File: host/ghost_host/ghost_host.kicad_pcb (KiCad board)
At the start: 2 copper layers, 13 parts, among them J14 Conn_01x04, J15 RJ12_Shielded, J16 Conn_01x06, U6 PCA9615DP

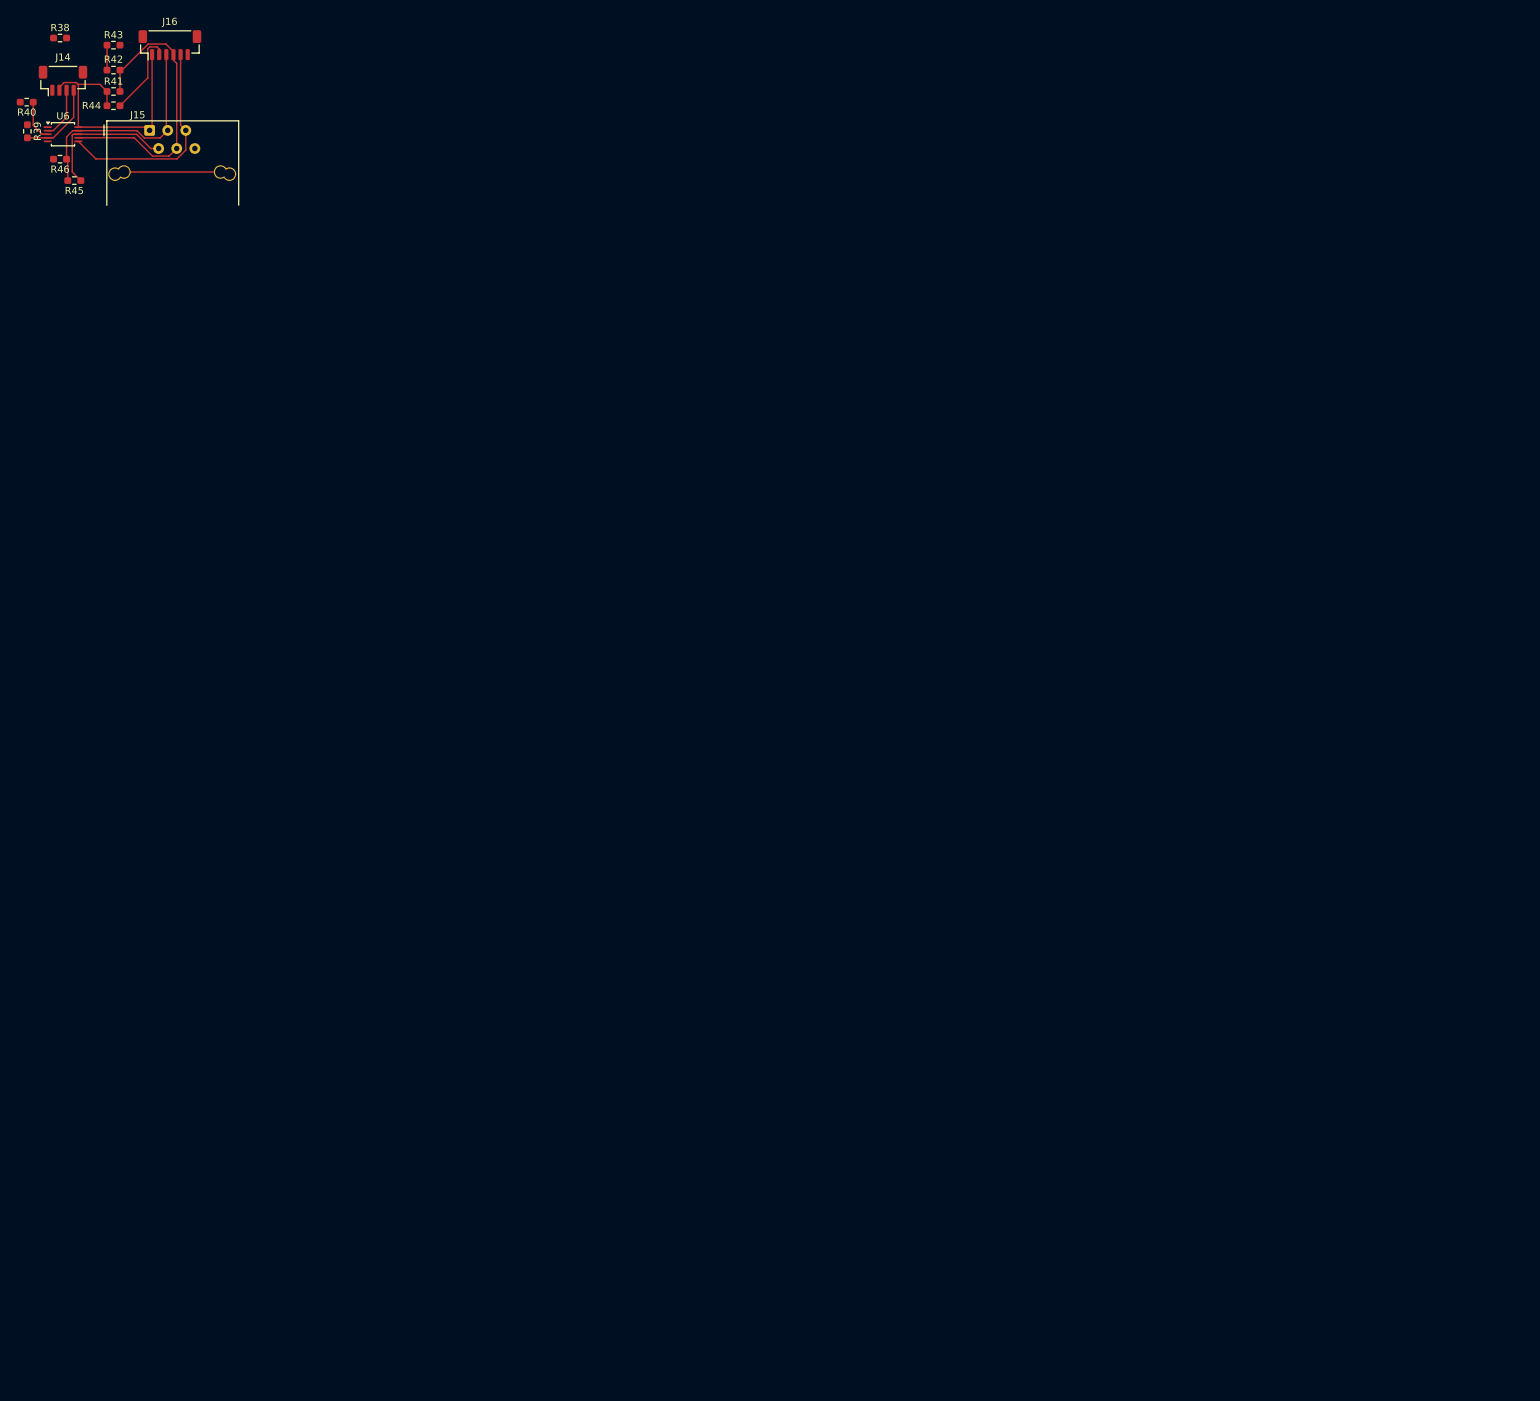
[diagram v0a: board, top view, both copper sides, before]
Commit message: finished host board PCB layout
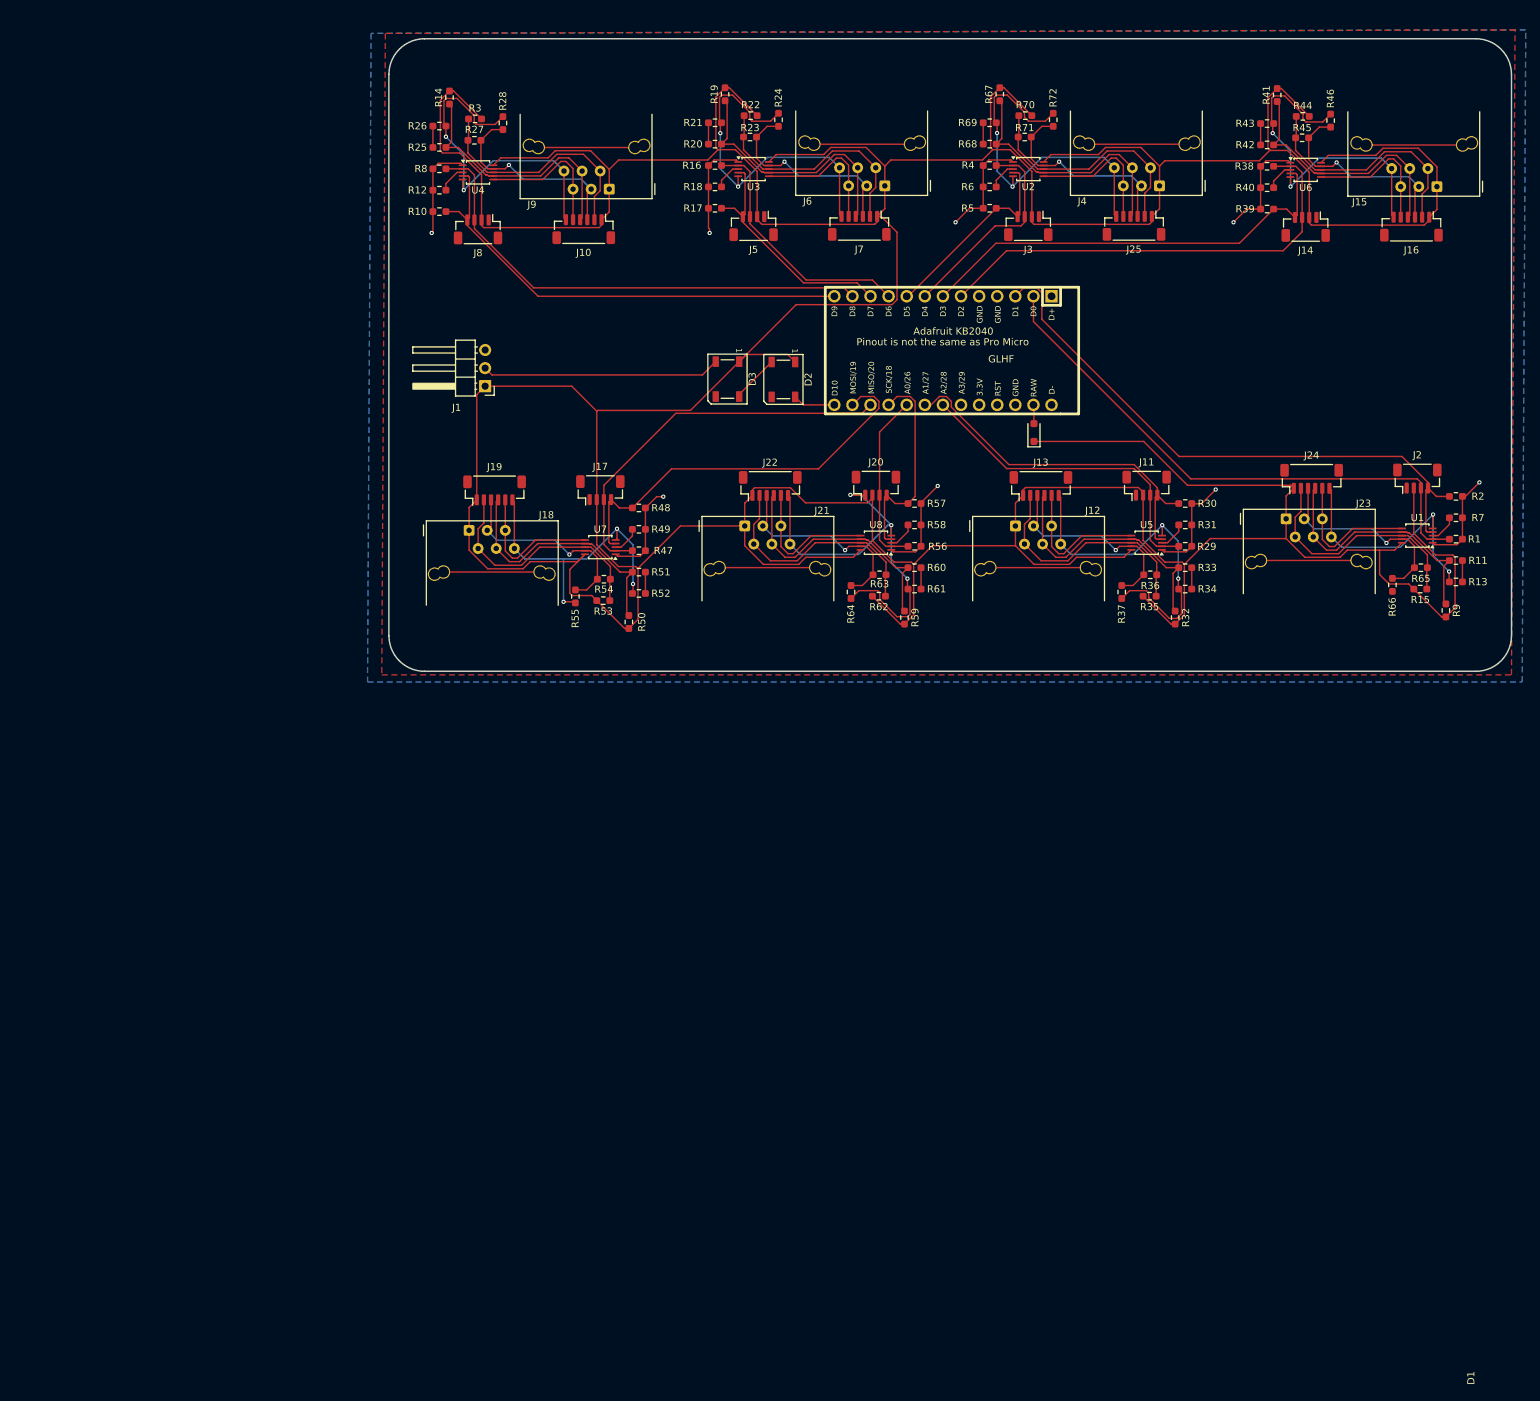
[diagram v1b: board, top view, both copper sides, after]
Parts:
- added D1: CMS06(TE12L,Q,M), Diode_SMD:D_SOD-323_HandSoldering, F.Cu at (165.0, 89.5)
- added D2: WS2812B, LED_SMD:LED_WS2812B_PLCC4_5.0x5.0mm_P3.2mm, F.Cu at (129.8, 82.0)
- added D3: WS2812B, LED_SMD:LED_WS2812B_PLCC4_5.0x5.0mm_P3.2mm, F.Cu at (122.0, 82.0)
- added J1: RGB_3_Pin_Connector, Connector_PinHeader_2.54mm:PinHeader_1x03_P2.54mm_Horizontal, F.Cu at (88.0, 83.0)
- added J10: Conn_01x06, Connector_JST:JST_SH_BM06B-SRSS-TB_1x06-1MP_P1.00mm_Vertical, F.Cu at (101.8, 61.0)
- added J11: Conn_01x04, Connector_JST:JST_SH_BM04B-SRSS-TB_1x04-1MP_P1.00mm_Vertical, F.Cu at (180.8, 97.0)
- added J12: RJ12_Shielded, RJ12_Pin_Connector:RJ12_Pin_Connector, F.Cu at (162.4, 102.6)
- added J13: Conn_01x06, Connector_JST:JST_SH_BM06B-SRSS-TB_1x06-1MP_P1.00mm_Vertical, F.Cu at (166.0, 97.0)
- added J17: Conn_01x04, Connector_JST:JST_SH_BM04B-SRSS-TB_1x04-1MP_P1.00mm_Vertical, F.Cu at (104.2, 97.6)
- added J18: RJ12_Shielded, RJ12_Pin_Connector:RJ12_Pin_Connector, F.Cu at (85.8, 103.2)
- added J19: Conn_01x06, Connector_JST:JST_SH_BM06B-SRSS-TB_1x06-1MP_P1.00mm_Vertical, F.Cu at (89.3, 97.6)
- added J2: Conn_01x04, Connector_JST:JST_SH_BM04B-SRSS-TB_1x04-1MP_P1.00mm_Vertical, F.Cu at (218.8, 96.0)
- added J20: Conn_01x04, Connector_JST:JST_SH_BM04B-SRSS-TB_1x04-1MP_P1.00mm_Vertical, F.Cu at (142.8, 97.0)
- added J21: RJ12_Shielded, RJ12_Pin_Connector:RJ12_Pin_Connector, F.Cu at (124.4, 102.6)
- added J22: Conn_01x06, Connector_JST:JST_SH_BM06B-SRSS-TB_1x06-1MP_P1.00mm_Vertical, F.Cu at (128.0, 97.0)
- added J23: RJ12_Shielded, RJ12_Pin_Connector:RJ12_Pin_Connector, F.Cu at (200.4, 101.6)
- added J24: Conn_01x06, Connector_JST:JST_SH_BM06B-SRSS-TB_1x06-1MP_P1.00mm_Vertical, F.Cu at (204.0, 96.0)
- added J25: Conn_01x06, Connector_JST:JST_SH_BM06B-SRSS-TB_1x06-1MP_P1.00mm_Vertical, F.Cu at (179.0, 60.5)
- added J3: Conn_01x04, Connector_JST:JST_SH_BM04B-SRSS-TB_1x04-1MP_P1.00mm_Vertical, F.Cu at (164.2, 60.5)
- added J4: RJ12_Shielded, RJ12_Pin_Connector:RJ12_Pin_Connector, F.Cu at (182.6, 54.9)
- added J5: Conn_01x04, Connector_JST:JST_SH_BM04B-SRSS-TB_1x04-1MP_P1.00mm_Vertical, F.Cu at (125.7, 60.5)
- added J6: RJ12_Shielded, RJ12_Pin_Connector:RJ12_Pin_Connector, F.Cu at (144.1, 54.9)
- added J7: Conn_01x06, Connector_JST:JST_SH_BM06B-SRSS-TB_1x06-1MP_P1.00mm_Vertical, F.Cu at (140.5, 60.5)
- added J8: Conn_01x04, Connector_JST:JST_SH_BM04B-SRSS-TB_1x04-1MP_P1.00mm_Vertical, F.Cu at (87.0, 61.0)
- added J9: RJ12_Shielded, RJ12_Pin_Connector:RJ12_Pin_Connector, F.Cu at (105.4, 55.4)
- added R1: 4.7k, Resistor_SMD:R_0603_1608Metric_Pad0.98x0.95mm_HandSolder, F.Cu at (224.2, 104.5)
- added R10: 4.7k, Resistor_SMD:R_0603_1608Metric_Pad0.98x0.95mm_HandSolder, F.Cu at (81.6, 58.5)
- added R11: 120, Resistor_SMD:R_0603_1608Metric_Pad0.98x0.95mm_HandSolder, F.Cu at (224.2, 107.5)
- added R12: 10k, Resistor_SMD:R_0603_1608Metric_Pad0.98x0.95mm_HandSolder, F.Cu at (81.6, 55.5)
- added R13: 600, Resistor_SMD:R_0603_1608Metric_Pad0.98x0.95mm_HandSolder, F.Cu at (224.2, 110.5)
- added R14: 600, Resistor_SMD:R_0603_1608Metric_Pad0.98x0.95mm_HandSolder, F.Cu at (83.0, 42.5)
- added R15: 600, Resistor_SMD:R_0603_1608Metric_Pad0.98x0.95mm_HandSolder, F.Cu at (219.2, 111.5)
- added R16: 4.7k, Resistor_SMD:R_0603_1608Metric_Pad0.98x0.95mm_HandSolder, F.Cu at (120.3, 52.0)
- added R17: 4.7k, Resistor_SMD:R_0603_1608Metric_Pad0.98x0.95mm_HandSolder, F.Cu at (120.3, 58.0)
- added R18: 10k, Resistor_SMD:R_0603_1608Metric_Pad0.98x0.95mm_HandSolder, F.Cu at (120.3, 55.0)
- added R19: 600, Resistor_SMD:R_0603_1608Metric_Pad0.98x0.95mm_HandSolder, F.Cu at (121.7, 42.0)
- added R2: 4.7k, Resistor_SMD:R_0603_1608Metric_Pad0.98x0.95mm_HandSolder, F.Cu at (224.2, 98.5)
- added R20: 120, Resistor_SMD:R_0603_1608Metric_Pad0.98x0.95mm_HandSolder, F.Cu at (120.3, 49.0)
- added R21: 600, Resistor_SMD:R_0603_1608Metric_Pad0.98x0.95mm_HandSolder, F.Cu at (120.3, 46.0)
- added R22: 600, Resistor_SMD:R_0603_1608Metric_Pad0.98x0.95mm_HandSolder, F.Cu at (125.3, 45.0)
- added R23: 120, Resistor_SMD:R_0603_1608Metric_Pad0.98x0.95mm_HandSolder, F.Cu at (125.2, 48.0)
- added R24: 600, Resistor_SMD:R_0603_1608Metric_Pad0.98x0.95mm_HandSolder, F.Cu at (129.2, 45.6)
- added R25: 120, Resistor_SMD:R_0603_1608Metric_Pad0.98x0.95mm_HandSolder, F.Cu at (81.6, 49.5)
- added R26: 600, Resistor_SMD:R_0603_1608Metric_Pad0.98x0.95mm_HandSolder, F.Cu at (81.6, 46.5)
- added R27: 120, Resistor_SMD:R_0603_1608Metric_Pad0.98x0.95mm_HandSolder, F.Cu at (86.5, 48.5)
- added R28: 600, Resistor_SMD:R_0603_1608Metric_Pad0.98x0.95mm_HandSolder, F.Cu at (90.5, 46.1)
- added R29: 4.7k, Resistor_SMD:R_0603_1608Metric_Pad0.98x0.95mm_HandSolder, F.Cu at (186.2, 105.5)
- added R3: 600, Resistor_SMD:R_0603_1608Metric_Pad0.98x0.95mm_HandSolder, F.Cu at (86.6, 45.5)
- added R30: 4.7k, Resistor_SMD:R_0603_1608Metric_Pad0.98x0.95mm_HandSolder, F.Cu at (186.2, 99.5)
- added R31: 10k, Resistor_SMD:R_0603_1608Metric_Pad0.98x0.95mm_HandSolder, F.Cu at (186.2, 102.5)
- added R32: 600, Resistor_SMD:R_0603_1608Metric_Pad0.98x0.95mm_HandSolder, F.Cu at (184.8, 115.5)
- added R33: 120, Resistor_SMD:R_0603_1608Metric_Pad0.98x0.95mm_HandSolder, F.Cu at (186.2, 108.5)
- added R34: 600, Resistor_SMD:R_0603_1608Metric_Pad0.98x0.95mm_HandSolder, F.Cu at (186.2, 111.5)
- added R35: 600, Resistor_SMD:R_0603_1608Metric_Pad0.98x0.95mm_HandSolder, F.Cu at (181.2, 112.5)
- added R36: 120, Resistor_SMD:R_0603_1608Metric_Pad0.98x0.95mm_HandSolder, F.Cu at (181.3, 109.5)
- added R37: 600, Resistor_SMD:R_0603_1608Metric_Pad0.98x0.95mm_HandSolder, F.Cu at (177.3, 111.9)
- added R4: 4.7k, Resistor_SMD:R_0603_1608Metric_Pad0.98x0.95mm_HandSolder, F.Cu at (158.8, 52.0)
- added R47: 4.7k, Resistor_SMD:R_0603_1608Metric_Pad0.98x0.95mm_HandSolder, F.Cu at (109.6, 106.1)
- added R48: 4.7k, Resistor_SMD:R_0603_1608Metric_Pad0.98x0.95mm_HandSolder, F.Cu at (109.6, 100.1)
- added R49: 10k, Resistor_SMD:R_0603_1608Metric_Pad0.98x0.95mm_HandSolder, F.Cu at (109.6, 103.1)
- added R5: 4.7k, Resistor_SMD:R_0603_1608Metric_Pad0.98x0.95mm_HandSolder, F.Cu at (158.8, 58.0)
- added R50: 600, Resistor_SMD:R_0603_1608Metric_Pad0.98x0.95mm_HandSolder, F.Cu at (108.2, 116.1)
- added R51: 120, Resistor_SMD:R_0603_1608Metric_Pad0.98x0.95mm_HandSolder, F.Cu at (109.6, 109.1)
- added R52: 600, Resistor_SMD:R_0603_1608Metric_Pad0.98x0.95mm_HandSolder, F.Cu at (109.6, 112.1)
- added R53: 600, Resistor_SMD:R_0603_1608Metric_Pad0.98x0.95mm_HandSolder, F.Cu at (104.6, 113.1)
- added R54: 120, Resistor_SMD:R_0603_1608Metric_Pad0.98x0.95mm_HandSolder, F.Cu at (104.7, 110.1)
- added R55: 600, Resistor_SMD:R_0603_1608Metric_Pad0.98x0.95mm_HandSolder, F.Cu at (100.7, 112.5)
- added R56: 4.7k, Resistor_SMD:R_0603_1608Metric_Pad0.98x0.95mm_HandSolder, F.Cu at (148.2, 105.5)
- added R57: 4.7k, Resistor_SMD:R_0603_1608Metric_Pad0.98x0.95mm_HandSolder, F.Cu at (148.2, 99.5)
- added R58: 10k, Resistor_SMD:R_0603_1608Metric_Pad0.98x0.95mm_HandSolder, F.Cu at (148.2, 102.5)
- added R59: 600, Resistor_SMD:R_0603_1608Metric_Pad0.98x0.95mm_HandSolder, F.Cu at (146.8, 115.5)
- added R6: 10k, Resistor_SMD:R_0603_1608Metric_Pad0.98x0.95mm_HandSolder, F.Cu at (158.8, 55.0)
- added R60: 120, Resistor_SMD:R_0603_1608Metric_Pad0.98x0.95mm_HandSolder, F.Cu at (148.2, 108.5)
- added R61: 600, Resistor_SMD:R_0603_1608Metric_Pad0.98x0.95mm_HandSolder, F.Cu at (148.2, 111.5)
- added R62: 600, Resistor_SMD:R_0603_1608Metric_Pad0.98x0.95mm_HandSolder, F.Cu at (143.2, 112.5)
- added R63: 120, Resistor_SMD:R_0603_1608Metric_Pad0.98x0.95mm_HandSolder, F.Cu at (143.3, 109.5)
- added R64: 600, Resistor_SMD:R_0603_1608Metric_Pad0.98x0.95mm_HandSolder, F.Cu at (139.3, 111.9)
- added R65: 120, Resistor_SMD:R_0603_1608Metric_Pad0.98x0.95mm_HandSolder, F.Cu at (219.3, 108.5)
- added R66: 600, Resistor_SMD:R_0603_1608Metric_Pad0.98x0.95mm_HandSolder, F.Cu at (215.3, 110.9)
- added R67: 600, Resistor_SMD:R_0603_1608Metric_Pad0.98x0.95mm_HandSolder, F.Cu at (160.2, 42.0)
- added R68: 120, Resistor_SMD:R_0603_1608Metric_Pad0.98x0.95mm_HandSolder, F.Cu at (158.8, 49.0)
- added R69: 600, Resistor_SMD:R_0603_1608Metric_Pad0.98x0.95mm_HandSolder, F.Cu at (158.8, 46.0)
- added R7: 10k, Resistor_SMD:R_0603_1608Metric_Pad0.98x0.95mm_HandSolder, F.Cu at (224.2, 101.5)
- added R70: 600, Resistor_SMD:R_0603_1608Metric_Pad0.98x0.95mm_HandSolder, F.Cu at (163.8, 45.0)
- added R71: 120, Resistor_SMD:R_0603_1608Metric_Pad0.98x0.95mm_HandSolder, F.Cu at (163.7, 48.0)
- added R72: 600, Resistor_SMD:R_0603_1608Metric_Pad0.98x0.95mm_HandSolder, F.Cu at (167.7, 45.6)
- added R8: 4.7k, Resistor_SMD:R_0603_1608Metric_Pad0.98x0.95mm_HandSolder, F.Cu at (81.6, 52.5)
- added R9: 600, Resistor_SMD:R_0603_1608Metric_Pad0.98x0.95mm_HandSolder, F.Cu at (222.8, 114.5)
- added U1: PCA9615DP, Package_SO:TSSOP-10_3x3mm_P0.5mm, F.Cu at (218.8, 104.0)
- added U2: PCA9615DP, Package_SO:TSSOP-10_3x3mm_P0.5mm, F.Cu at (164.2, 52.5)
- added U3: PCA9615DP, Package_SO:TSSOP-10_3x3mm_P0.5mm, F.Cu at (125.7, 52.5)
- added U4: PCA9615DP, Package_SO:TSSOP-10_3x3mm_P0.5mm, F.Cu at (87.0, 53.0)
- added U5: PCA9615DP, Package_SO:TSSOP-10_3x3mm_P0.5mm, F.Cu at (180.8, 105.0)
- added U7: PCA9615DP, Package_SO:TSSOP-10_3x3mm_P0.5mm, F.Cu at (104.2, 105.6)
- added U8: PCA9615DP, Package_SO:TSSOP-10_3x3mm_P0.5mm, F.Cu at (142.8, 105.0)
- added U9: kb2040, kb2040:kb2040, F.Cu at (153.5, 78.0)
- moved J15 180.8 mm to (221.5, 55.0), turned to 180 degrees
- moved R46 178.3 mm to (206.6, 45.7), turned to 90 degrees
- moved J16 176.0 mm to (218.0, 60.6), turned to 180 degrees
- moved J14 175.6 mm to (203.1, 60.6), turned to 180 degrees
- moved R40 174.4 mm to (197.7, 55.1)
- moved U6 174.4 mm to (203.1, 52.6)
- moved R39 174.3 mm to (197.7, 58.1), turned to 0 degrees
- moved R45 172.4 mm to (202.6, 48.1), turned to 0 degrees
- moved R38 170.3 mm to (197.7, 52.1)
- moved R44 166.9 mm to (202.7, 45.1), turned to 180 degrees
- moved R41 163.3 mm to (199.1, 42.1), turned to -90 degrees
- moved R43 162.2 mm to (197.7, 46.1)
- moved R42 162.2 mm to (197.7, 49.1)
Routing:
- net +5V: track 37.2 -> 818.8 mm
- net GND: track 0.00 -> 385.6 mm, vias 0 -> 18
- net +3.3V: track 0.00 -> 114.7 mm, vias 0 -> 8
- net /scl1: track 0.00 -> 83.3 mm
- net /sda1: track 0.00 -> 78.7 mm
- net /sda5: track 0.00 -> 68.8 mm
- net /scl5: track 0.00 -> 67.0 mm
- net /sda2: track 7.23 -> 64.3 mm
- net /scl8: track 0.00 -> 56.5 mm
- net /sda8: track 0.00 -> 54.8 mm
- net /scl2: track 11.5 -> 62.1 mm
- net /scl6: track 0.00 -> 50.6 mm
- net /sda6: track 0.00 -> 45.9 mm
- net Net-(J25-Pin_4): track 0.00 -> 36.1 mm
- net Net-(J13-Pin_4): track 0.00 -> 36.1 mm
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- added copper zone on B.Cu, net +3.3V
- added copper zone on F.Cu, net GND
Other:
- board outline added: 157.5 x 88.8 mm

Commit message: reorg pcb layout
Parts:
- added H1: MountingHole_Pad, MountingHole:MountingHole_4.5mm_Pad_Via, F.Cu at (132.5, 150.0)
- added H2: MountingHole_Pad, MountingHole:MountingHole_4.5mm_Pad_Via, F.Cu at (132.5, 160.5)
- added H3: MountingHole_Pad, MountingHole:MountingHole_4.5mm_Pad_Via, F.Cu at (132.5, 171.1)
- added H4: MountingHole_Pad, MountingHole:MountingHole_4.5mm_Pad_Via, F.Cu at (132.5, 181.6)
- moved U6 319.2 mm to (-25.9, 274.9), turned to 180 degrees
- moved R41 315.2 mm to (-20.3, 268.4), turned to 180 degrees
- moved R38 312.5 mm to (-20.3, 276.0), turned to 180 degrees
- moved R44 310.3 mm to (-20.3, 260.9)
- moved U2 309.4 mm to (-50.9, 274.9), turned to 180 degrees
- moved R46 309.3 mm to (-20.3, 255.9), turned to 180 degrees
- moved R43 307.8 mm to (-20.3, 263.4), turned to 180 degrees
- moved R42 307.4 mm to (-20.3, 265.9)
- moved R40 306.8 mm to (-20.3, 271.0)
- moved R45 306.4 mm to (-20.3, 258.4), turned to 180 degrees
- moved R39 306.4 mm to (-20.3, 273.5), turned to 180 degrees
- moved R67 305.8 mm to (-45.3, 268.4), turned to 180 degrees
- moved R4 303.0 mm to (-45.3, 276.0), turned to 180 degrees
- moved R70 300.5 mm to (-45.3, 260.9)
- moved U3 300.2 mm to (-75.9, 274.9), turned to 180 degrees
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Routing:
- net +5V: track 818.8 -> 0.00 mm
- net GND: track 385.6 -> 0.00 mm, vias 18 -> 0
- net +3.3V: track 114.7 -> 0.00 mm, vias 8 -> 0
- net /scl1: track 83.3 -> 0.00 mm
- net /sda1: track 78.7 -> 0.00 mm
- net /sda5: track 68.8 -> 0.00 mm
- net /scl5: track 67.0 -> 0.00 mm
- net /sda2: track 64.3 -> 0.00 mm
- net /scl2: track 62.1 -> 0.00 mm
- net /scl8: track 56.5 -> 0.00 mm
- net /sda8: track 54.8 -> 0.00 mm
- net /scl6: track 50.6 -> 0.00 mm
- net /sda6: track 45.9 -> 0.00 mm
- net Net-(J25-Pin_4): track 36.1 -> 0.00 mm
- net Net-(J13-Pin_4): track 36.1 -> 0.00 mm
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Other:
- board size 157.5 x 88.8 mm -> 98.5 x 79 mm
- board text added: "holes need to be same spacing as vex c-channel"

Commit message: make things nicerg
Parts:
- added H5: MountingHole_Pad, MountingHole:MountingHole_4.5mm_Pad_Via, F.Cu at (79.3, 182.0)
- added H6: MountingHole_Pad, MountingHole:MountingHole_4.5mm_Pad_Via, F.Cu at (92.0, 182.0)
- D1, R1, R10, R11, R12, R13, R14, R15, R16, R17, R18, R19, R2, R20, R21, R22, R23, R24, R25, R26, R27, R28, R29, R3, R30, R31, R32, R33, R34, R35, R36, R37, R38, R39, R4, R40, R41, R42, R43, R44, R45, R46, R47, R48, R49, R5, R50, R51, R52, R53, R54, R55, R56, R57, R58, R59, R6, R60, R61, R62, R63, R64, R65, R66, R67, R68, R69, R7, R70, R71, R72, R8, R9, U1, U2, U3, U4, U5, U6, U7, U8, U9: moved to B.Cu
- moved R56 159.9 mm to (43.2, 200.0), turned to 180 degrees
- moved R57 159.9 mm to (43.2, 202.5), turned to 180 degrees
- moved R58 159.9 mm to (43.2, 205.0), turned to 180 degrees
- moved R2 159.4 mm to (94.0, 202.5), turned to 180 degrees
- moved R30 159.4 mm to (69.0, 202.5), turned to 180 degrees
- moved R31 159.4 mm to (69.0, 205.0), turned to 180 degrees
- moved R48 159.4 mm to (19.0, 202.5), turned to 180 degrees
- moved R49 159.4 mm to (19.0, 205.0), turned to 180 degrees
- moved R7 159.4 mm to (94.0, 205.0), turned to 180 degrees
- moved R1 159.4 mm to (94.0, 200.0), turned to 180 degrees
- moved R29 159.4 mm to (69.0, 200.0), turned to 180 degrees
- moved R47 159.4 mm to (19.0, 200.0), turned to 180 degrees
- moved U8 157.7 mm to (51.0, 200.0), turned to 180 degrees
- moved U1 157.2 mm to (101.7, 200.0), turned to 180 degrees
- moved U5 157.2 mm to (76.7, 200.0), turned to 180 degrees
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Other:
- board size 98.5 x 79 mm -> 127.5 x 68.5 mm
- board text added: "CH 0"
- board text added: "plz double check that the holes r half inch spacing"
- board text removed: "holes need to be same spacing as vex c-channel"

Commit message: finished host board
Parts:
- U9: value kb2040 -> ProMicro
- moved R49 199.3 mm to (190.6, 103.7), turned to 0 degrees
- moved R48 196.9 mm to (190.6, 105.9)
- moved R47 192.6 mm to (183.9, 100.4), turned to -90 degrees
- moved R50 184.1 mm to (190.6, 107.9), turned to 180 degrees
- moved J19 183.5 mm to (178.4, 100.2)
- moved J18 183.5 mm to (180.9, 110.3)
- moved U7 183.5 mm to (184.1, 105.6), turned to -90 degrees
- moved J17 183.5 mm to (189.1, 100.2)
- moved R53 183.5 mm to (177.9, 105.7)
- moved R51 181.5 mm to (190.6, 110.4)
- moved R52 179.0 mm to (190.6, 112.9), turned to 180 degrees
- moved R24 174.9 mm to (164.1, 68.7), turned to 0 degrees
- moved R54 173.9 mm to (177.9, 109.9)
- moved R23 171.0 mm to (164.1, 66.4)
- moved R55 169.4 mm to (177.9, 107.7), turned to 180 degrees
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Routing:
- net GND: track 0.00 -> 537.0 mm, vias 0 -> 15
- net +3.3V: track 0.00 -> 232.3 mm, vias 0 -> 8
- net +5V: track 0.00 -> 157.1 mm, vias 0 -> 16
- net /scl8: track 0.00 -> 78.6 mm, vias 0 -> 3
- net /sda8: track 0.00 -> 75.7 mm, vias 0 -> 3
- net /sda5: track 0.00 -> 66.3 mm, vias 0 -> 2
- net /scl5: track 0.00 -> 64.5 mm, vias 0 -> 2
- net /sda7: track 0.00 -> 59.6 mm, vias 0 -> 2
- net /scl7: track 0.00 -> 56.2 mm, vias 0 -> 1
- net /sda4: track 0.00 -> 49.0 mm, vias 0 -> 2
- net /scl4: track 0.00 -> 48.7 mm, vias 0 -> 2
- net /sda6: track 0.00 -> 44.5 mm, vias 0 -> 2
- net Net-(D3-DOUT): track 0.00 -> 44.0 mm
- net /scl1: track 0.00 -> 41.2 mm, vias 0 -> 2
- net /sda1: track 0.00 -> 40.9 mm, vias 0 -> 1
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- added copper zone on F.Cu, net +5V
- added copper zone on B.Cu, net GND
- removed copper zone on F.Cu, net GND
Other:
- outline, holes or cut-outs redrawn
- board text removed: "CH 0"
